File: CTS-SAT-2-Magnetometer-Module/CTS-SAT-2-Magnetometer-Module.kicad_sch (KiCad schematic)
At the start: 31 parts, among them J2 SWD, J3 SWD, SW1 SW_Push, U1 MMC5983MA, U2 LIS2MDL, U3 STM32F072C8Tx, U4 MIC5365-3.3YD5

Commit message: Re-routed
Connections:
- net DRDY: now also U3.20 (PB2); no longer U3.21 (PB10)
- net INT: now also U3.21 (PB10); no longer U3.20 (PB2)
- net SWDCLK: now also U3.33 (PA12); no longer U3.37 (PA14)
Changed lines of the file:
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@@
-	)
-	(no_connect
-		(at 35.56 123.19)
 	)
 	(no_connect
@@
 	)
 	(no_connect
+		(at 35.56 118.11)
+	)
+	(no_connect
 		(at 35.56 143.51)
 	)
@@
 	(wire
 		(pts
-			(xy 68.58 120.65) (xy 78.74 120.65)
-		)
-		(stroke
-			(width 0)
-			(type default)
-		)
-	)
-	(wire
-		(pts
 			(xy 72.39 143.51) (xy 76.2 143.51)
 		)
@@
 	(wire
 		(pts
-			(xy 31.75 118.11) (xy 35.56 118.11)
-		)
-		(stroke
-			(width 0)
-			(type default)
-		)
-	)
-	(wire
-		(pts
 			(xy 45.72 168.91) (xy 45.72 158.75)
 		)
@@
 	(wire
 		(pts
+			(xy 74.93 100.33) (xy 68.58 100.33)
+		)
+		(stroke
+			(width 0)
+			(type default)
+		)
+	)
+	(wire
+		(pts
 			(xy 237.49 64.77) (xy 247.65 64.77)
 		)
@@
 	(wire
 		(pts
+			(xy 31.75 123.19) (xy 35.56 123.19)
+		)
+		(stroke
+			(width 0)
+			(type default)
+		)
+	)
+	(wire
+		(pts
 			(xy 251.46 127) (xy 256.54 127)
 		)
@@
 	(wire
 		(pts
-			(xy 71.12 100.33) (xy 68.58 100.33)
-		)
-		(stroke
-			(width 0)
-			(type default)
-		)
-	)
-	(wire
-		(pts
 			(xy 107.95 38.1) (xy 107.95 40.64)
 		)
@@
 	(wire
 		(pts
+			(xy 76.2 120.65) (xy 68.58 120.65)
+		)
+		(stroke
+			(width 0)
+			(type default)
+		)
+	)
+	(wire
+		(pts
 			(xy 91.44 140.97) (xy 91.44 143.51)
 		)
@@
 	(global_label "SWDCLK"
 		(shape input)
-		(at 31.75 118.11 180)
+		(at 31.75 123.19 180)
 		(fields_autoplaced yes)
 		(effects
@@
 		)
 		(property "Intersheetrefs" "${INTERSHEET_REFS}"
-			(at 21.2658 118.11 0)
+			(at 21.2658 123.19 0)
 			(hide yes)
 			(show_name no)
@@
 	(global_label "DRDY"
 		(shape input)
-		(at 71.12 100.33 0)
+		(at 76.2 120.65 0)
 		(fields_autoplaced yes)
 		(effects
@@
 		)
 		(property "Intersheetrefs" "${INTERSHEET_REFS}"
-			(at 79.0038 100.33 0)
+			(at 84.0838 120.65 0)
 			(hide yes)
 			(show_name no)
@@
 	(global_label "INT"
 		(shape input)
-		(at 78.74 120.65 0)
+		(at 74.93 100.33 0)
 		(fields_autoplaced yes)
 		(effects
@@
 		)
 		(property "Intersheetrefs" "${INTERSHEET_REFS}"
-			(at 84.6281 120.65 0)
-			(hide yes)
-			(show_name no)
+			(at 80.8181 100.33 0)
+			(hide yes)
+			(show_name no)

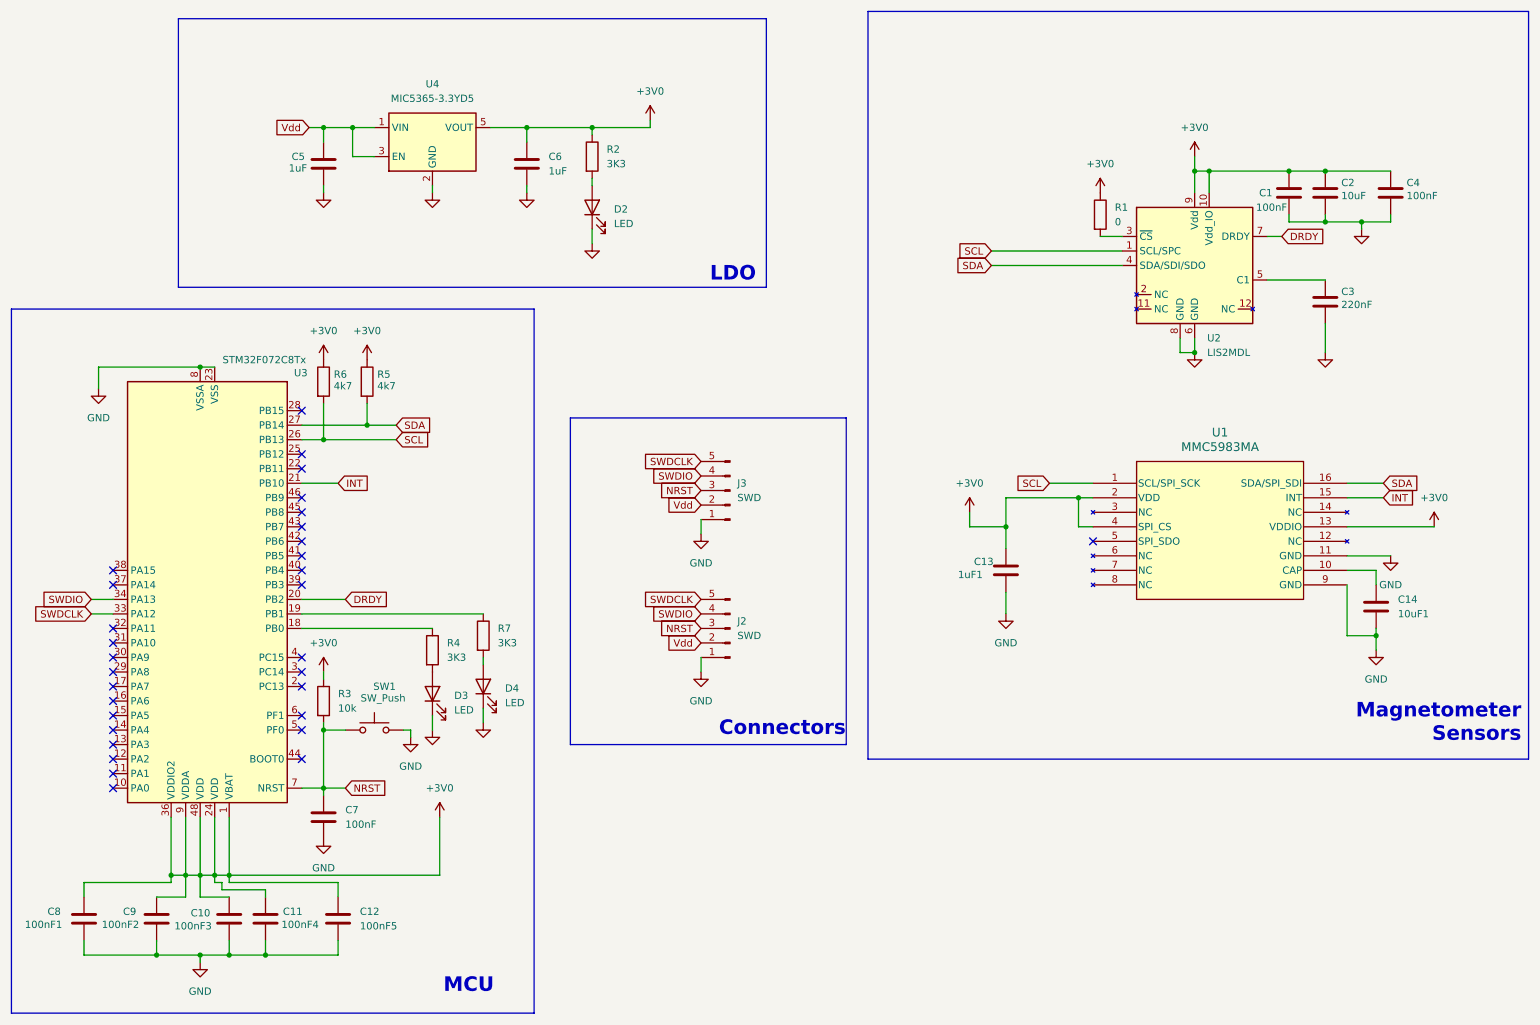
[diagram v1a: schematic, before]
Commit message: Applied Changes for schematic rev 2
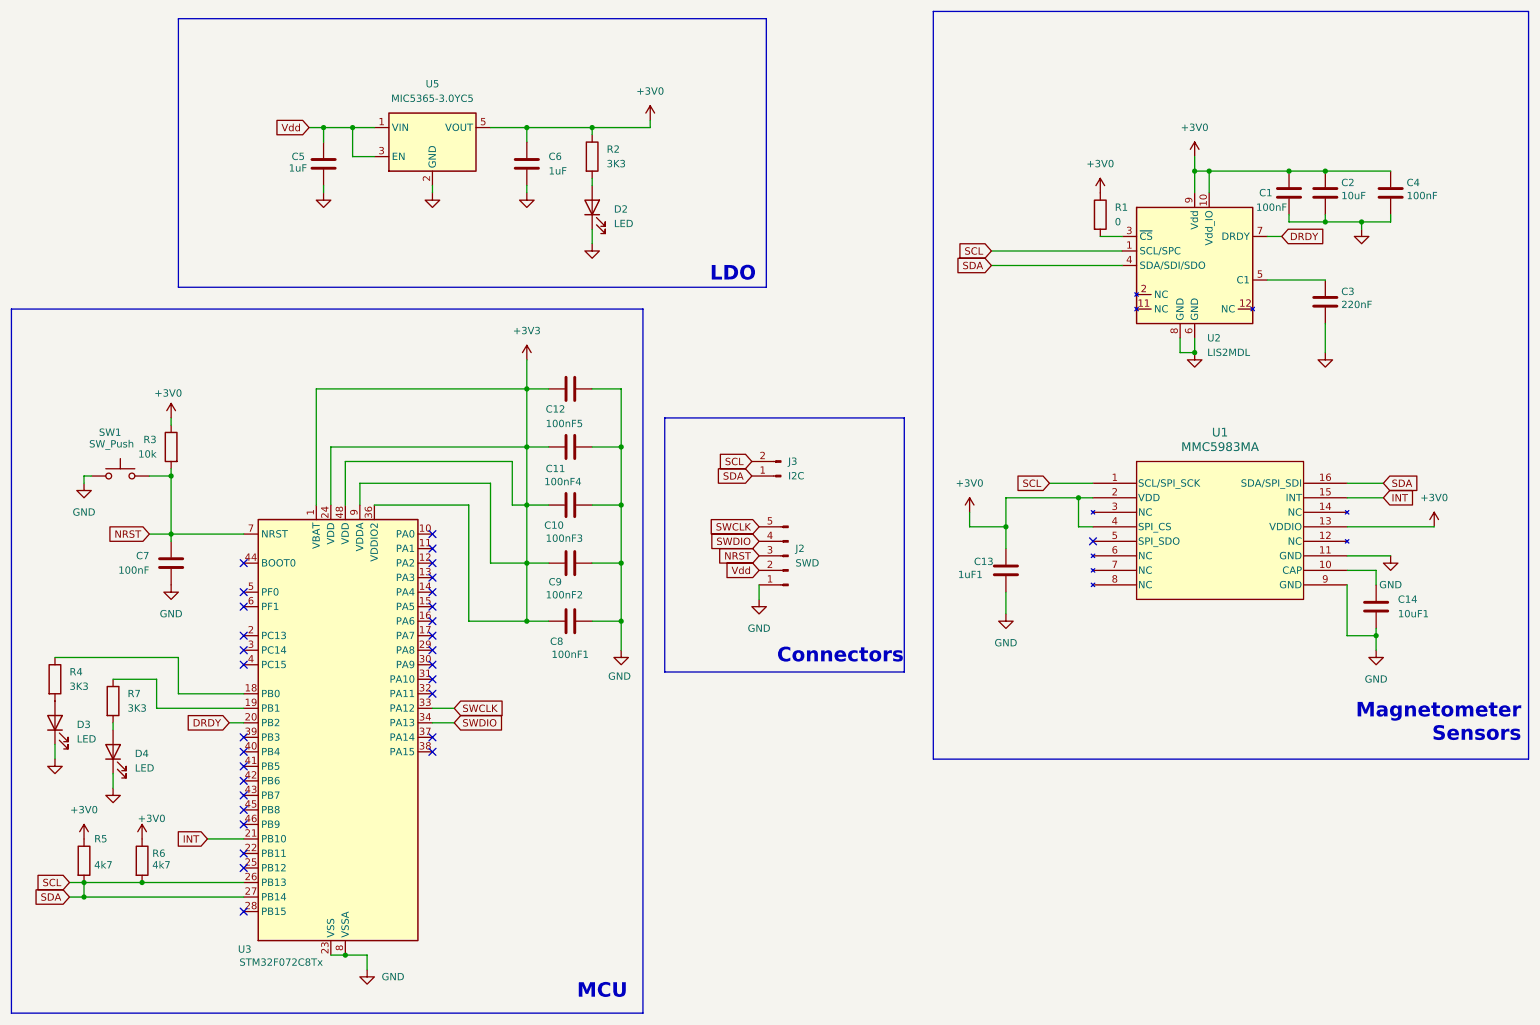
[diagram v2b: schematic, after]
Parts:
- removed J3: SWD, Connector_PinHeader_2.54mm:PinHeader_1x05_P2.54mm_Vertical, symbol Connector:Conn_01x05_Pin
- removed U4: MIC5365-3.3YD5, Package_TO_SOT_SMD:SOT-23-5, symbol Regulator_Linear:MIC5365-3.3YD5
- added J3: I2C, Connector_PinHeader_2.54mm:PinHeader_1x02_P2.54mm_Vertical, symbol Connector:Conn_01x02_Pin
- added U5: MIC5365-3.0YC5, Package_TO_SOT_SMD:SOT-353_SC-70-5, symbol Regulator_Linear:MIC5365-3.0YC5
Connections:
- net SDA is gone; now on net SCL: R5.2, U1.16 (SDA/SPI_SDI), U2.4 (SDA/SDI/SDO), U3.27 (PB14)
- net +3V0: now also U5.5 (VOUT); no longer C10.2, C11.2, C12.1, C8.2, C9.2, U3.1 (VBAT), U3.24 (VDD), U3.36 (VDDIO2), U3.48 (VDD), U3.9 (VDDA)
- net GND: now also C9.2, U5.2 (GND); no longer C9.1
- net SCL: now also J3.1 (Pin_1), J3.2 (Pin_2)
- net Vdd: now also U5.1 (VIN), U5.3 (EN)
- net SWDCLK renamed SWCLK
- new net +3V3: C10.2, C11.2, C12.1, C8.2, C9.1, U3.1 (VBAT), U3.24 (VDD), U3.36 (VDDIO2), U3.48 (VDD), U3.9 (VDDA)
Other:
- moved on the sheet: C10, C11, C12, C7, C8, C9, D3, D4, J2, R3, R4, R5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
